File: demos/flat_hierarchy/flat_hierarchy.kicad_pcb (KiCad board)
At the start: 2 copper layers, 68 parts, among them J1 DB9-FEMAL, P1 CONN_2, P2 SUPP28, P3 SUPP40, Q1 BC237, Q2 BC307, Q3 BC307, U1 24Cxx, U2 74HC125, U3 7805, U4 LT1373, U5 PIC_18_PINS, U6 PIC_8_PINS

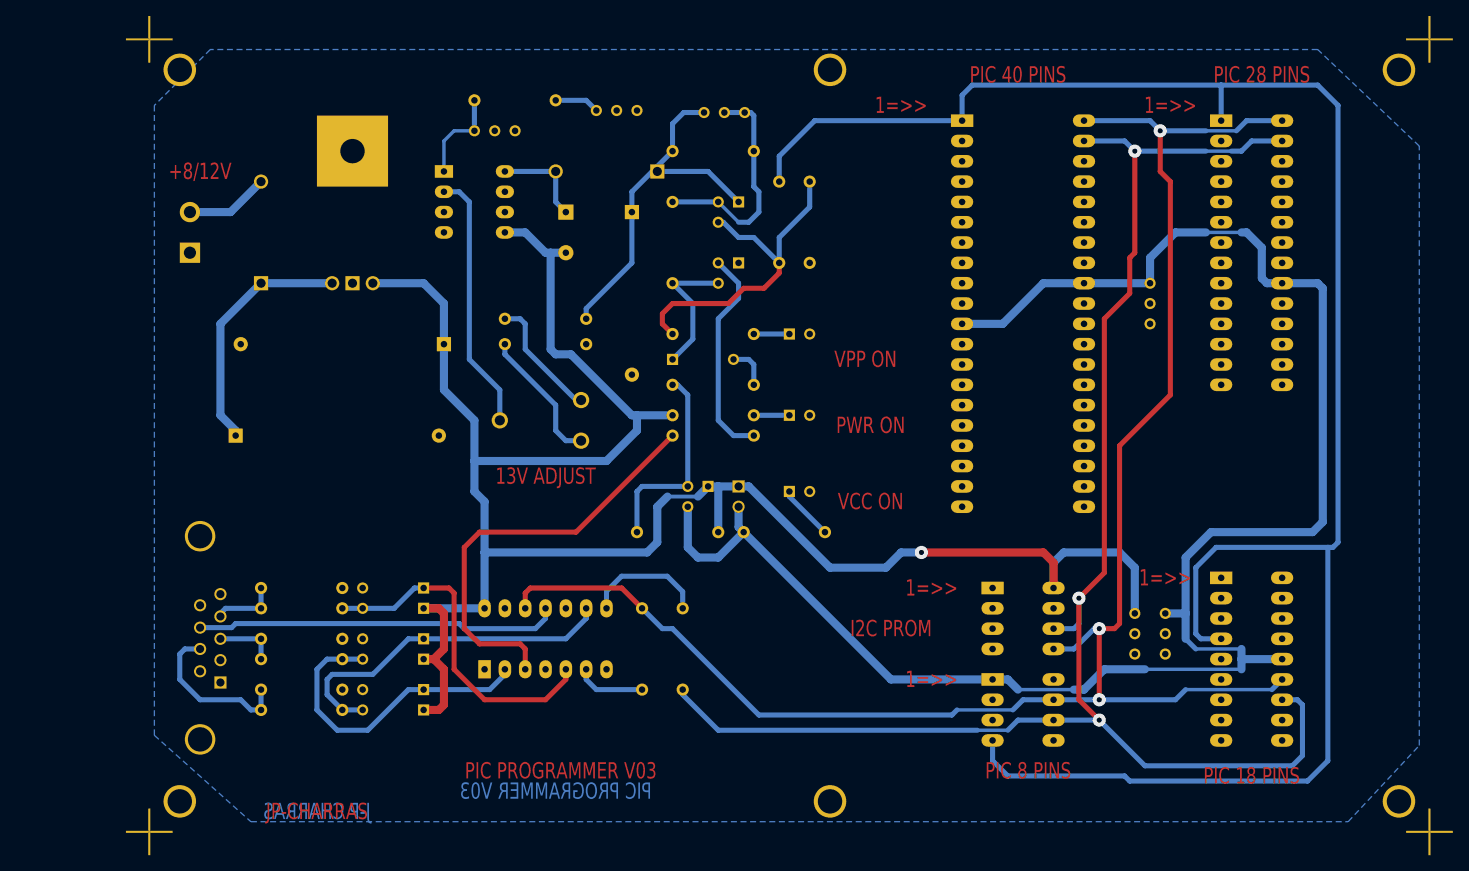
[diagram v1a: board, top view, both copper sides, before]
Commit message: Update old demo board files. Minor code cleaning.
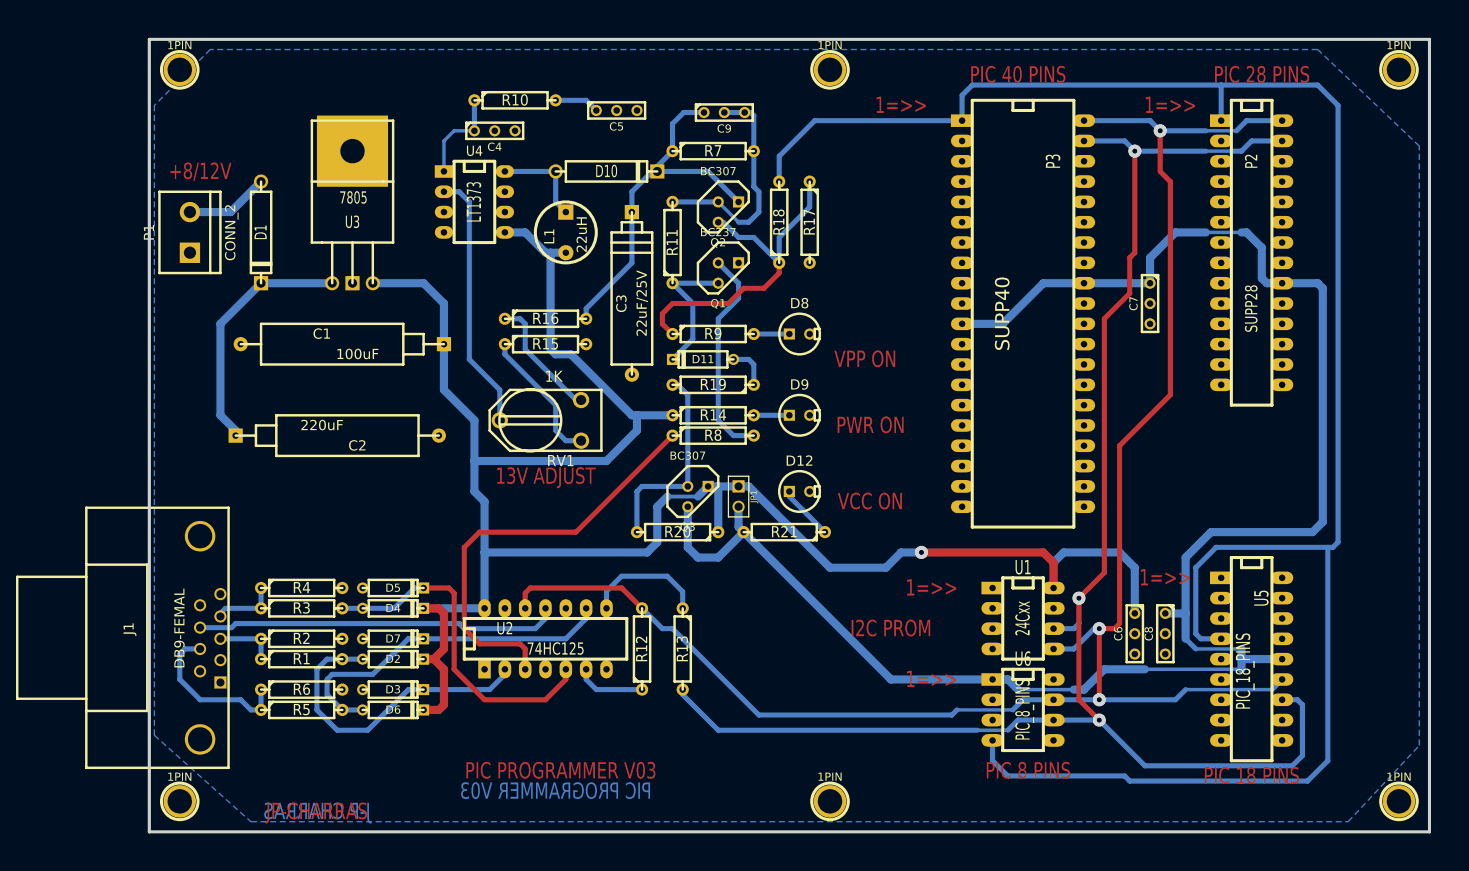
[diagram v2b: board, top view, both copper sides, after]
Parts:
- removed MIRE (x4): *, MIRE
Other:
- board outline added: 160 x 99.1 mm

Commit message: Update demo files
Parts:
- C1, C2: footprint CP10 -> discret:CP10
- C3: footprint CP8 -> discret:CP8
- C4, C5, C6, C7, C8, C9: footprint C1-1 -> discret:C1-1
- D1, D10: footprint D5 -> discret:D5
- D11, D2, D3, D4, D5, D6, D7: footprint D3 -> discret:D3
- D12, D8, D9: footprint LEDV -> discret:LEDV
- J1: footprint DB9FC -> connect:DB9FC
- JP1: footprint PIN_ARRAY_2X1 -> pin_array:PIN_ARRAY_2X1
- L1: footprint INDUCTOR_V -> inductors:INDUCTOR_V
- P1: footprint bornier2 -> connect:bornier2
- Q1, Q2, Q3: footprint TO92 -> discret:TO92
- R1, R10, R11, R12, R13, R14, R15, R16, R17, R18, R19, R2, R20, R21, R3, R4, R5, R6, R7, R8, R9: footprint R4 -> discret:R4
- RV1: footprint RV2X4 -> discret:RV2X4
- U1, U4, U6: footprint 8DIP-ELL300 -> dip_sockets:DIP-8__300_ELL
- U2: footprint 14DIP-ELL300 -> dip_sockets:DIP-14__300_ELL
- U3: footprint LM78XX -> discret:LM78XX
- U5: footprint 18DIP-ELL300 -> dip_sockets:DIP-18__300_ELL
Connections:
- net /pic_programmer/PC-DATA-OUT renamed /pic_programmer/DTR
- net /pic_programmer/RTS renamed /pic_programmer/PC-CLOCK-OUT
- net /sockets/CLOCK-RB6 renamed CLOCK-RB6
- net /sockets/DATA-RB7 renamed DATA-RB7
- net /sockets/VCC_PIC renamed VCC_PIC
- P2 pad 1: /sockets/VPP-MCLR -> VPP-MCLR
- P3 pad 1: /sockets/VPP-MCLR -> VPP-MCLR
- R18 pad 2: N-000030 -> VPP-MCLR
- U5 pad 4: /sockets/VPP-MCLR -> VPP-MCLR
- U6 pad 4: /sockets/VPP-MCLR -> VPP-MCLR
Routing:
- net VPP-MCLR: track 0.00 -> 242.7 mm
- net /sockets/VPP-MCLR: track 239.5 -> 0.00 mm
- net N-000030: track 3.18 -> 0.00 mm
